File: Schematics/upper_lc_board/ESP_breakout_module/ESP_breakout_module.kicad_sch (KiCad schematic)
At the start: 26 parts, among them J8 USB_C_Female_USB2_Small, U1 ESP32-S3-WROOM-1-N16R2, U2 CAN_TRX_SN65HVD230DR, U3 PD_D3V3XA4B10LP

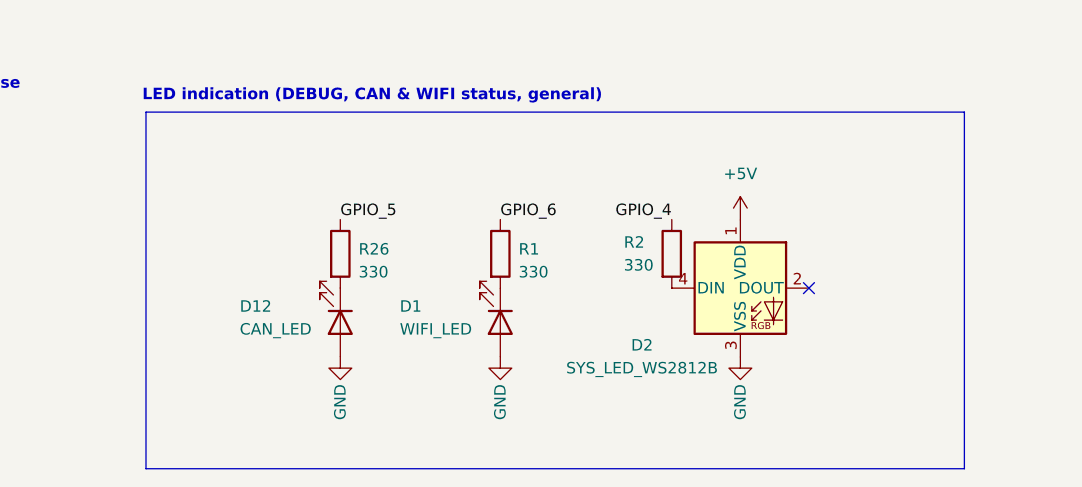
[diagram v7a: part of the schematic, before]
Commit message: more layout work, add FAULT LED
next: revert to ideal diode circuitry instead of MUX IC.
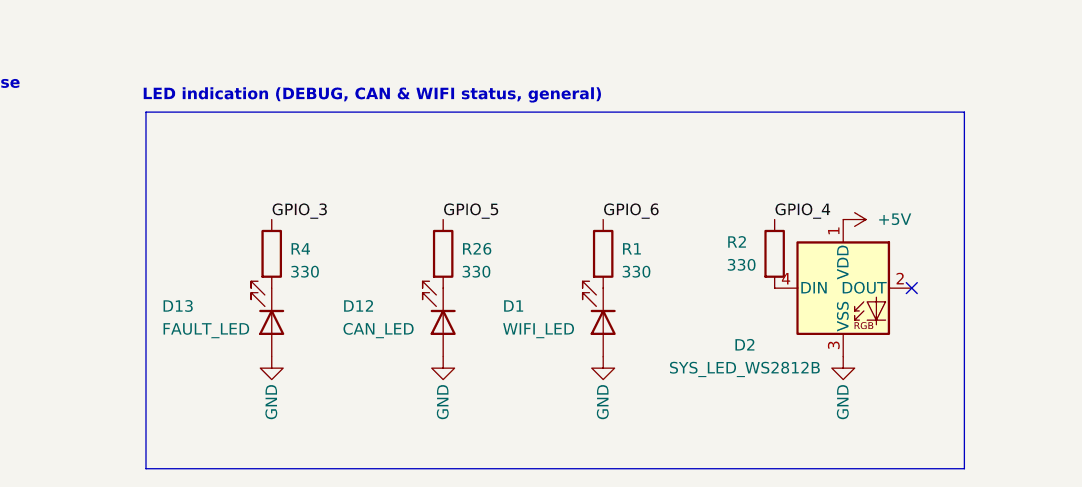
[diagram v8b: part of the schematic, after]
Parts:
- added D13: FAULT_LED, LED_SMD:LED_1206_3216Metric, symbol Device:LED
- added R4: 330, Resistor_SMD:R_0402_1005Metric, symbol Device:R
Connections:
- net GND: now also D13.2 (A)
- net GPIO_3: now also R4.1
- new net: D13.1 (K), R4.2
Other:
- moved on the sheet: D1, D12, D2, R1, R2, R26
